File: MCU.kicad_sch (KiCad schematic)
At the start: 47 parts, among them J7 Conn_01x04, J8 PinHeader_2x5_P1.27mm_SMD, SW1 SW_KSC441J70SHLFS_SMD, SW2 SW_KSC441J70SHLFS_SMD, U3 STM32U585CIT3, Y1 Oscillator_40MHz_YIC_OSC-S5

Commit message: Update footprint for testpoints
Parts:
- TP30, TP31, TP32, TP33, TP34, TP35, TP36: footprint Hardware Components Footprints:TP_2.54mm_THT_Keystone_500x -> TestPoint:TestPoint_Pad_1.5x1.5mm

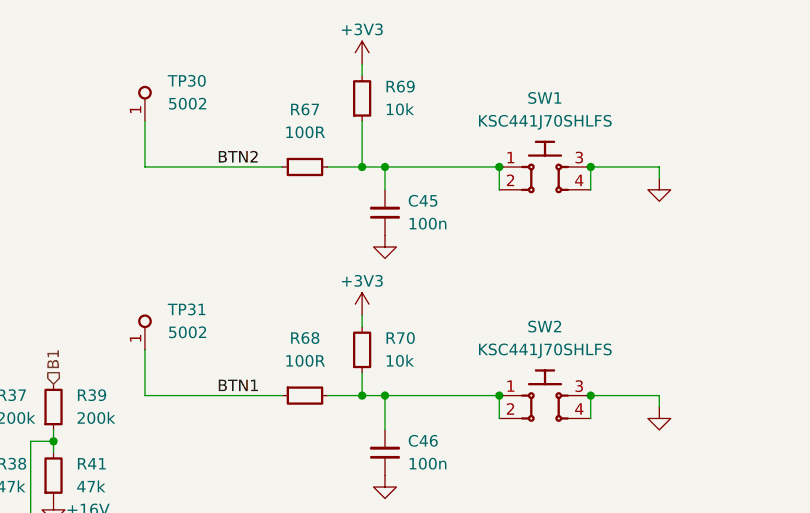
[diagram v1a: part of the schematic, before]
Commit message: Remove redundant resistors
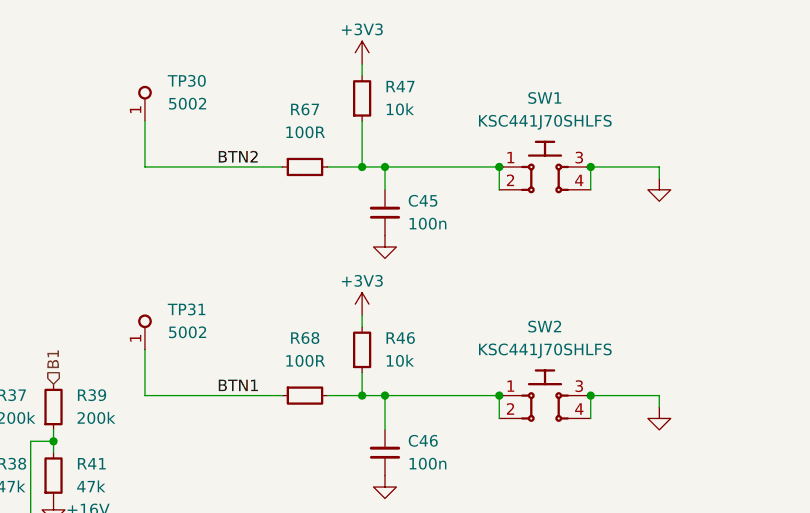
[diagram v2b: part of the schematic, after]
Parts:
- removed R69, R70: R_10k_0.1%_0402, Hardware Components Footprints:R_0402_1005Metric, symbol lib:R_10k_0.1%_0402
- added R46, R47: R_10k_0402, Hardware Components Footprints:R_0402_1005Metric, symbol lib:R_10k_0402
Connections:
- net +3V3: now also R46.2, R47.2
- net at C46.2, R68.2, SW2.1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: now also R46.1
- net at C45.2, R67.2, SW1.1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: now also R47.1

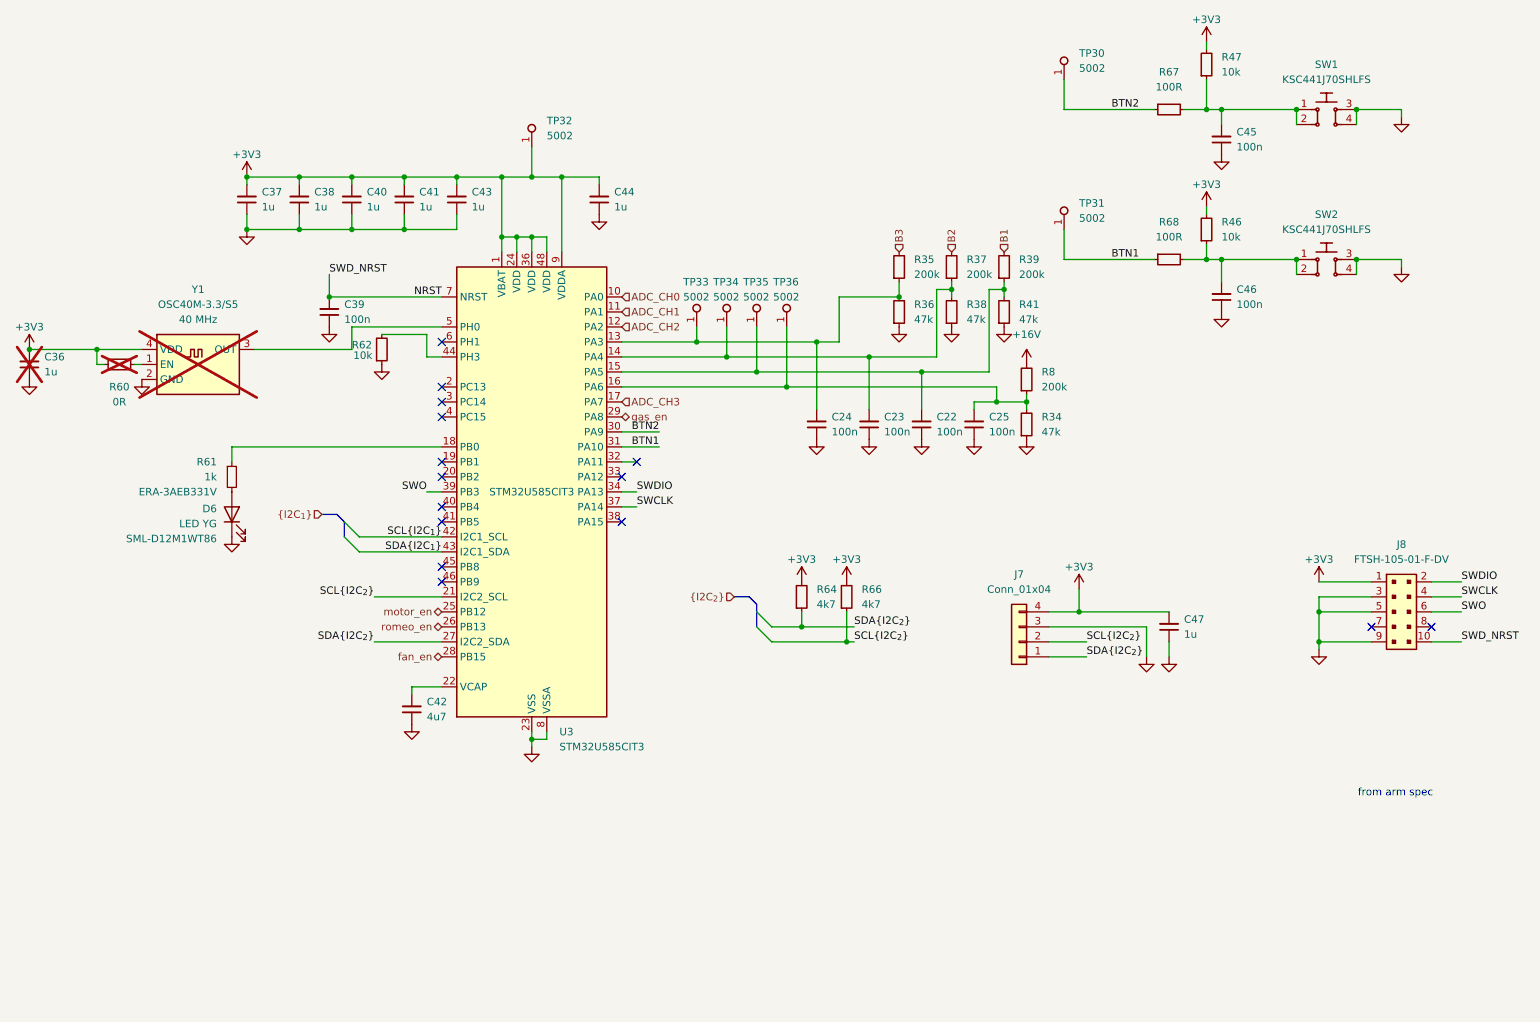
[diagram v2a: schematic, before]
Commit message: Add lead compensator, move leds to uC, redo resistors
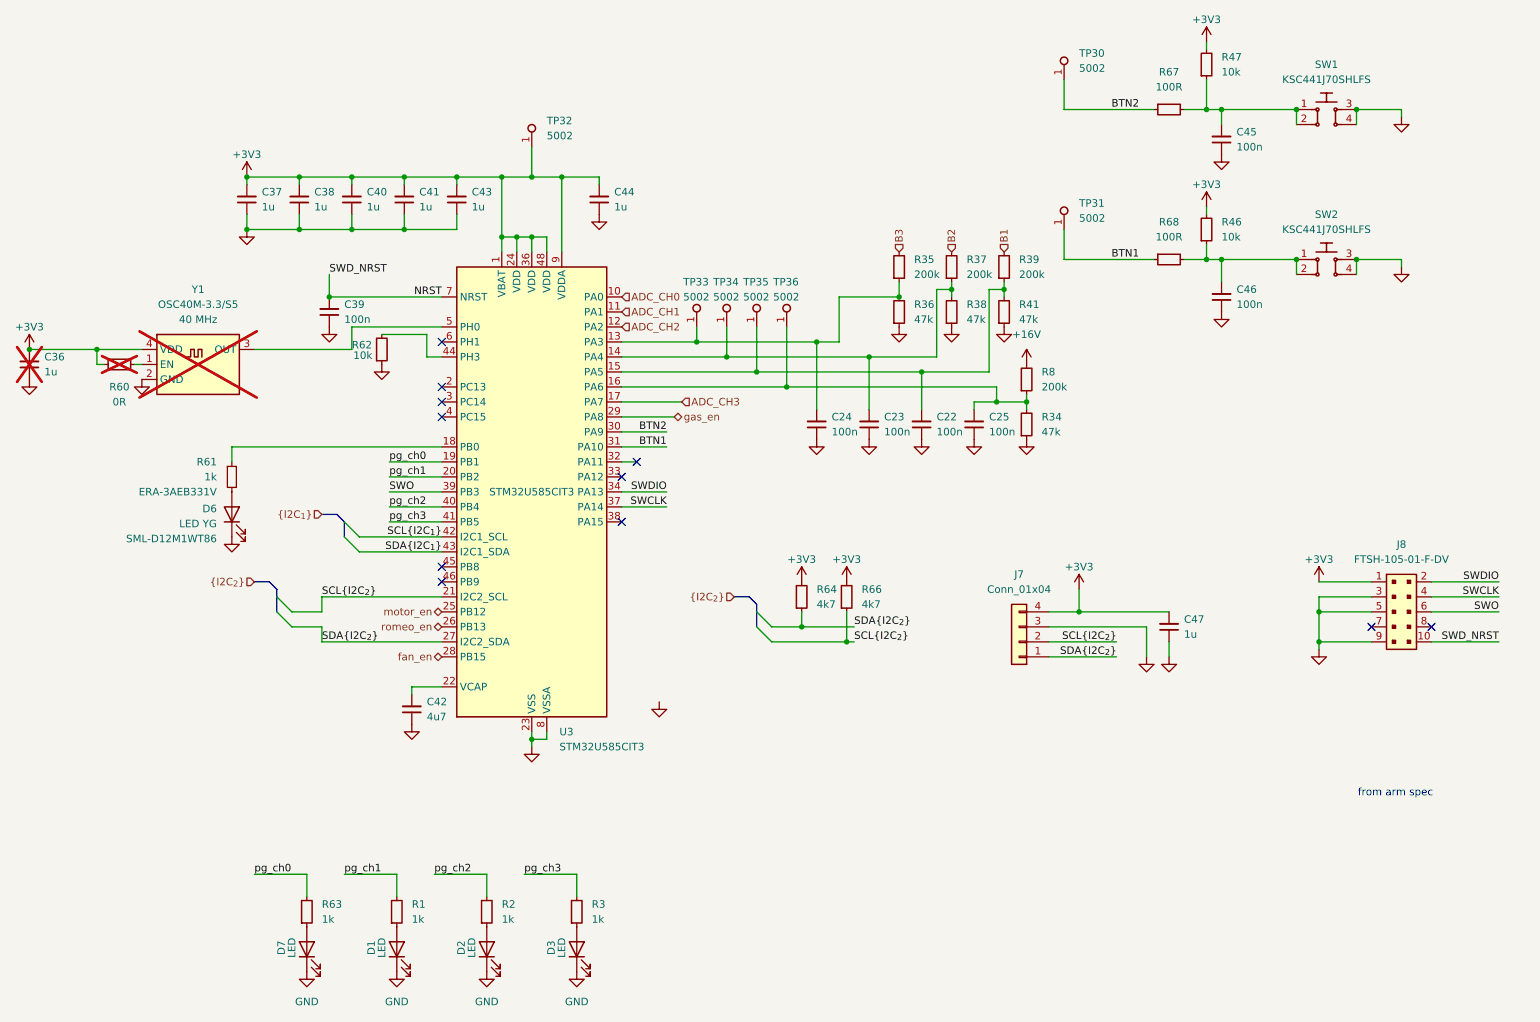
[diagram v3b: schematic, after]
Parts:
- added D1, D2, D3, D7: LED, LED_SMD:LED_0603_1608Metric, symbol lib:LED
- added R1, R2, R3, R63: R_1k_0402, Hardware Components Footprints:R_0402_1005Metric, symbol Hardware Components:R_1k_0402
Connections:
- net GND: now also D1.1 (K), D2.1 (K), D3.1 (K), D7.1 (K)
- net pg_ch0: now reaches U3.19 (PB1)
- net pg_ch0: now also R63.2
- net pg_ch1: now reaches U3.20 (PB2)
- net pg_ch1: now also R1.2
- net pg_ch2: now reaches U3.40 (PB4)
- net pg_ch2: now also R2.2
- net pg_ch3: now reaches U3.41 (PB5)
- net pg_ch3: now also R3.2
- new net: D2.2 (A), R2.1
- new net: D1.2 (A), R1.1
- new net: D3.2 (A), R3.1
- new net: D7.2 (A), R63.1
- no-connect marks 15 -> 11

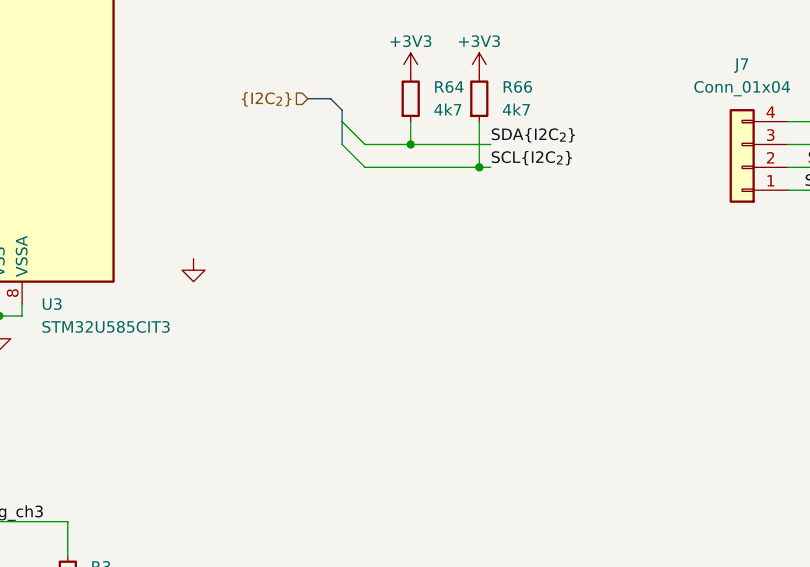
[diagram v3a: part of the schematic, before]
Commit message: add pull ups, fix lead compensator
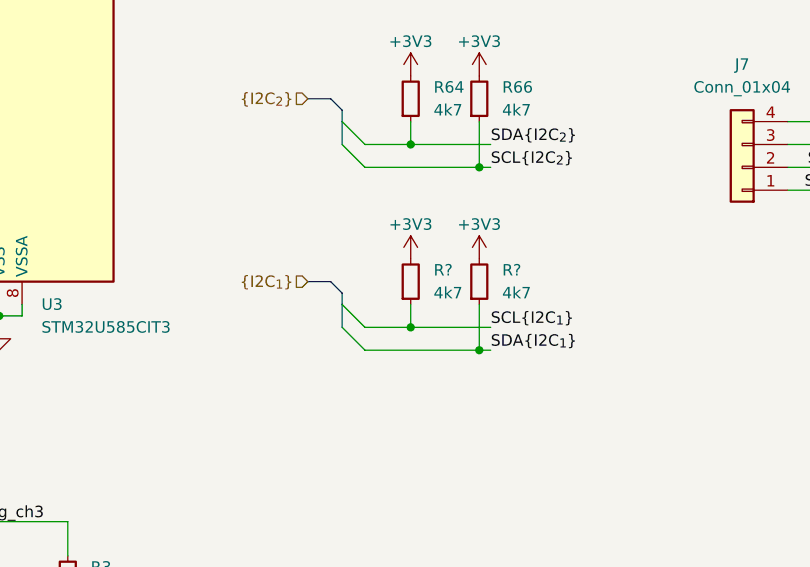
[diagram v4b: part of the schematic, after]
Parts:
- renumbered R66 to R?
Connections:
- net SCL{I2C_{1}}: now also R64.1
- net SDA{I2C_{1}}: now also R?.1
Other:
- moved on the sheet: R?

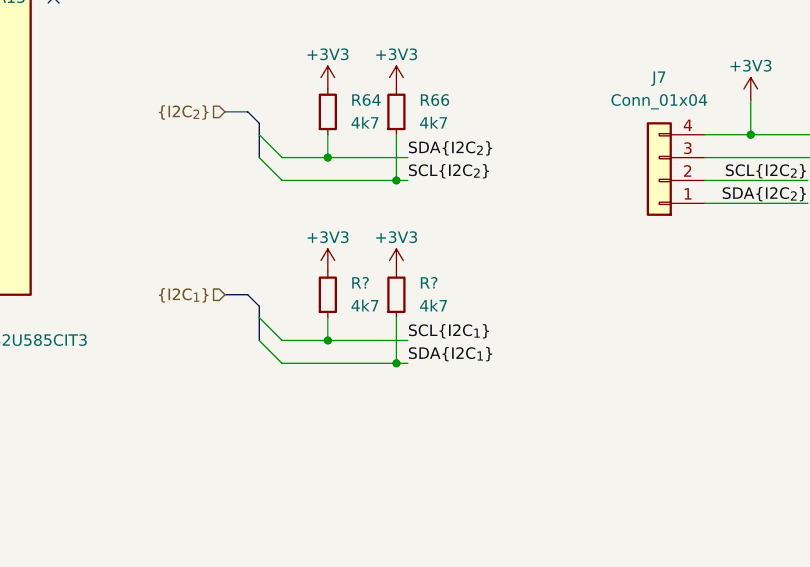
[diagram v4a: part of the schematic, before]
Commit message: update inductor
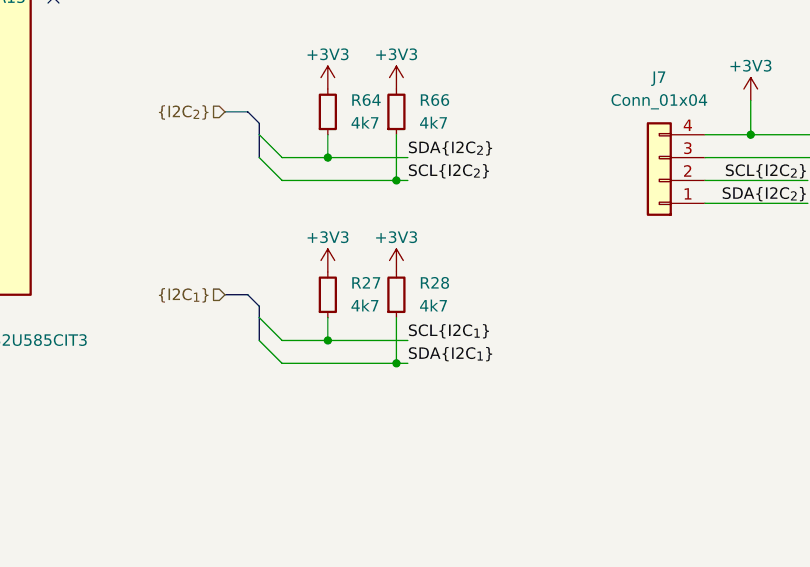
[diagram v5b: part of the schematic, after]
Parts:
- added R28, R64: R_4k7_0402, Hardware Components Footprints:R_0402_1005Metric, symbol lib:R_4k7_0402
- gave numbers to parts that had none: 1
- renumbered R64 to R27
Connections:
- net +3V3: now also R28.2, R64.2
- net SDA{I2C_{1}}: now also R28.1; no longer R66.1
- net SDA{I2C_{2}}: now also R64.1; no longer R27.1
